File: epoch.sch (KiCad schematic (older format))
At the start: 34 parts, among them J1 USB_OTG, J2 CONN_01X05, J3 CONN_01X02, P3 CONN_01X10, SW1 SW_Reset, U1 MIC5219-3.3BM5, U2 ATSAMD21Ennc-AU, U3 DS3231MZ, U4 MCP7940N-I/SN, U5 74HC1G14GW, U6 MH2mm, U7 MH2mm, U8 MH2mm, U9 MH2mm

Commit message: Remove connector and redo the connections
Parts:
- removed J3: CONN_01X02, Pin_Headers:Pin_Header_Straight_1x02_Pitch1.27mm, symbol CONN_01X02
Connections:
- net labels removed: +3.3V(BATT), +3.3V(REGUL)
- wire segments 110 -> 105
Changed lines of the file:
@@
 Wire Wire Line
 	6650 950  6650 850
-Wire Wire Line
-	4800 2300 4950 2300
-Text GLabel 5050 1250 2    60   Output ~ 0
-+3.3V(REGUL)
 Text GLabel 2550 4400 0    60   Input ~ 0
 SWDIO
@@
 Wire Wire Line
 	8800 5600 9000 5600
-Text GLabel 4950 2300 2    60   Output ~ 0
-+3.3V(BATT)
 Text GLabel 2550 4500 0    60   Input ~ 0
 SWDCLK
-$Comp
-L CONN_01X02 J3
-U 1 1 5A087ADC
-P 10750 5550
-F 0 "J3" H 10750 5700 50  0000 C CNN
-F 1 "CONN_01X02" V 10850 5550 50  0000 C CNN
-F 2 "Pin_Headers:Pin_Header_Straight_1x02_Pitch1.27mm" H 10750 5550 50  0001 C CNN
-F 3 "" H 10750 5550 50  0001 C CNN
-	1    10750 5550
-	1    0    0    -1
-$EndComp
-Text GLabel 10450 5500 0    60   Input ~ 0
-+3.3V(REGUL)
-Text GLabel 10450 5650 0    60   Input ~ 0
-+3.3V(BATT)
-Wire Wire Line
-	10550 5500 10450 5500
-Wire Wire Line
-	10550 5600 10500 5600
-Wire Wire Line
-	10500 5600 10500 5650
-Wire Wire Line
-	10500 5650 10450 5650
 $Comp
 L (GND) #PWR033
@@
 Wire Wire Line
 	5300 7100 5400 7100
+$Comp
+L (+3.3) #PWR034
+U 1 1 5BC006BD
+P 4800 2300
+F 0 "#PWR034" H 4800 2350 30  0001 C CNN
+F 1 "(+3.3)" H 4800 2400 50  0000 C CNN
+F 2 "" H 4800 2300 60  0000 C CNN
+F 3 "" H 4800 2300 60  0000 C CNN
+	1    4800 2300
+	1    0    0    -1
+$EndComp
+$Comp
+L (+3.3) #PWR035
+U 1 1 5BC00ACB
+P 5050 1250
+F 0 "#PWR035" H 5050 1300 30  0001 C CNN
+F 1 "(+3.3)" H 5050 1350 50  0000 C CNN
+F 2 "" H 5050 1250 60  0000 C CNN
+F 3 "" H 5050 1250 60  0000 C CNN
+	1    5050 1250
+	1    0    0    -1
+$EndComp
 $EndSCHEMATC

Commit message: Update for LIPO power_board
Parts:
- removed BT1: Battery_Cell, Connectors:CR2032-001, symbol Battery_Cell
- removed C11, C2: 0.1uF, Capacitors_SMD:C_0805_HandSoldering, symbol C_Small
- removed P3: CONN_01X10, my-fp-library:MOLEX_0.5MM_505278, symbol CONN_01X10
- removed SW1: SW_Reset, Buttons_Switches_SMD:SW_SPST_B3U-3000P, symbol SW_Push
- removed U1: MIC5219-3.3BM5, TO_SOT_Packages_SMD:SOT-23-5, symbol AP131-33
- removed U5: 74HC1G14GW, TO_SOT_Packages_SMD:SOT-353_SC-70-5_Handsoldering, symbol 74HC1G14GW
- added C11, C2: 0.1uF, Capacitors_SMD:C_0805_HandSoldering, symbol Device:C_Small
- added J3: CONN_01X05, my-fp-library:Pin_Header_Straight_1x05_Pitch1.27mm_no_silk, symbol conn:CONN_01X05
- added P3: CONN_01X10, my-fp-library:MOLEX_0.5MM_505278, symbol conn:CONN_01X10
- added SW1: SW_Reset, Buttons_Switches_SMD:SW_SPST_B3U-3000P, symbol switches:SW_Push
- added U1: MIC5219-3.3BM5, TO_SOT_Packages_SMD:SOT-23-5, symbol regul:AP131-33
- added U5: 74HC1G14GW, TO_SOT_Packages_SMD:SOT-353_SC-70-5_Handsoldering, symbol marks:74HC1G14GW
- C1, C14, C3, C4, C5, C6, C9: symbol C_Small -> Device:C_Small
- D1: symbol LED -> Device:LED
- DOWN1, MID1, UP1: symbol Tact_SW_3x6x33.5 -> marks:Tact_SW_3x6x33.5
- J1: symbol USB_OTG -> conn:USB_OTG
- J2: symbol CONN_01X05 -> conn:CONN_01X05
- R1, R2, R3, R4, R5, R6: symbol R -> Device:R
- U2: symbol ATSAMD21Ennc-AU -> Atmel:ATSAMD21Ennc-AU
- U3: symbol DS3231MZ -> maxim:DS3231MZ
- U4: symbol MCP7940N-I/SN -> epoch-rescue:MCP7940N-I_SN
- U6, U7, U8, U9: symbol MH2.1mm -> marks:MH2.1mm
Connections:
- net (+3.3): now also C11.1, C2.1, P3.5 (P5), P3.6 (P6), P3.7 (P7), U1.5 (OUT), U5.5 (VCC)
- net (GND): now also C11.2, C2.2, J3.1 (P1), P3.10 (P10), P3.9 (P9), SW1.2, U1.2 (GND), U5.3 (GND)
- net EXTMODE: now also P3.8 (P8)
- net SPI_CLK: now also P3.1 (P1)
- net SPI_CS: now also P3.3 (P3)
- net SPI_SI: now also P3.2 (P2)
- net VCOM: now also P3.4 (P4), U5.4 (Y)
- net STAT: now reaches U2.11 (PA08)
- net STAT: now also J3.3 (P3)
- net PWR_SENSE: now reaches U2.8 (PA07)
- net PWR_SENSE: now also J3.2 (P2)
- net at C5.2: now also U1.4 (BP)
- net at R1.1: now also SW1.1
- net at R5.2, U4.7 (MFP): now also U5.2 (A)
- net VCC renamed VSS
- net VSS: now also J3.4 (P4)
- new net (+5): J3.5 (P5), U1.1 (IN), U1.3 (EN)
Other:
- moved on the sheet: C1, C14, C3, C4, C5, C6, C9, DOWN1, J1, MID1, R1, R2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

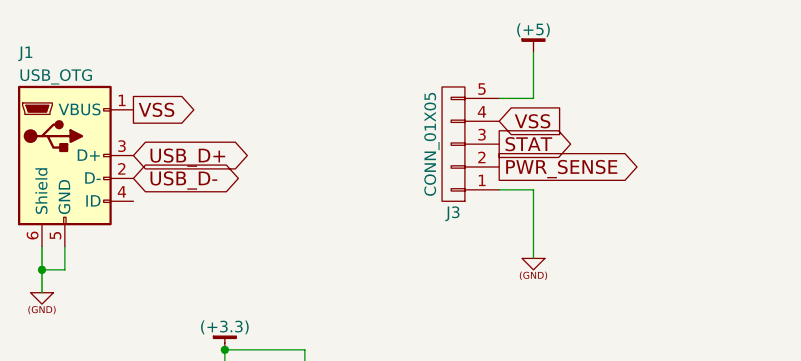
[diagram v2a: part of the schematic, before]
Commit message: New connections to power board
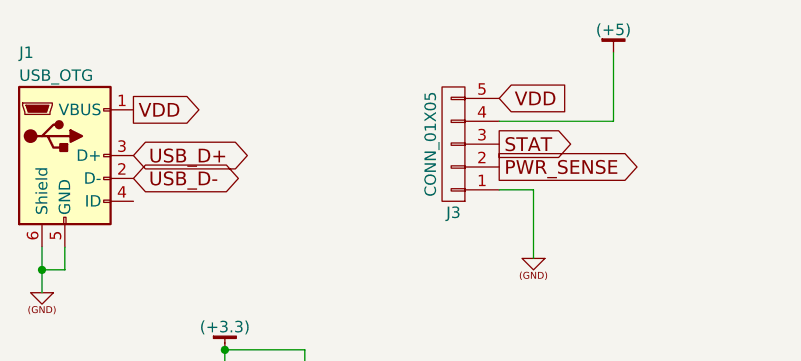
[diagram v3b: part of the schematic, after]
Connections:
- net (+5): now also J3.4 (P4); no longer J3.5 (P5)
- net VSS renamed VDD
- net VDD: now also J3.5 (P5); no longer J3.4 (P4)
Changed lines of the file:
@@
 $EndComp
 Text GLabel 1200 1200 2    60   Output ~ 0
-VSS
+VDD
 $Comp
 L conn:CONN_01X05 J3
@@
 	-1   0    0    -1
 $EndComp
-Text GLabel 2800 1250 2    60   Input ~ 0
-VSS
+Text GLabel 2800 1150 2    60   Input ~ 0
+VDD
 Text GLabel 2800 1350 2    60   Output ~ 0
 STAT
@@
 L power1:(+5) #PWR0102
 U 1 1 5C2AB633
-P 2950 950
-F 0 "#PWR0102" H 2950 1000 30  0001 C CNN
-F 1 "(+5)" H 2950 1050 50  0000 C CNN
-F 2 "" H 2950 950 60  0000 C CNN
-F 3 "" H 2950 950 60  0000 C CNN
-	1    2950 950
+P 3300 950
+F 0 "#PWR0102" H 3300 1000 30  0001 C CNN
+F 1 "(+5)" H 3300 1050 50  0000 C CNN
+F 2 "" H 3300 950 60  0000 C CNN
+F 3 "" H 3300 950 60  0000 C CNN
+	1    3300 950
 	1    0    0    -1
 $EndComp
@@
 Wire Wire Line
 	2950 1550 2950 1850
-Wire Wire Line
-	2800 1150 2950 1150
-Wire Wire Line
-	2950 1150 2950 950
 Text GLabel 3250 3500 2    60   Input ~ 0
 STAT
 Text GLabel 3250 3400 2    60   Input ~ 0
 PWR_SENSE
+Wire Wire Line
+	2800 1250 3300 1250
+Wire Wire Line
+	3300 1250 3300 950
 $EndSCHEMATC

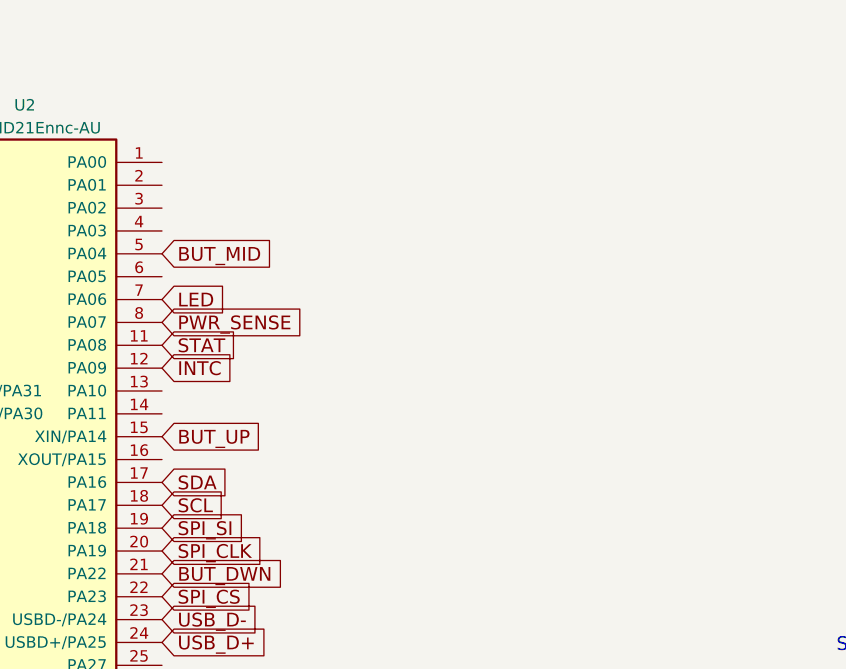
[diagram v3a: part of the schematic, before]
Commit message: Update for voltage divider to get battery level
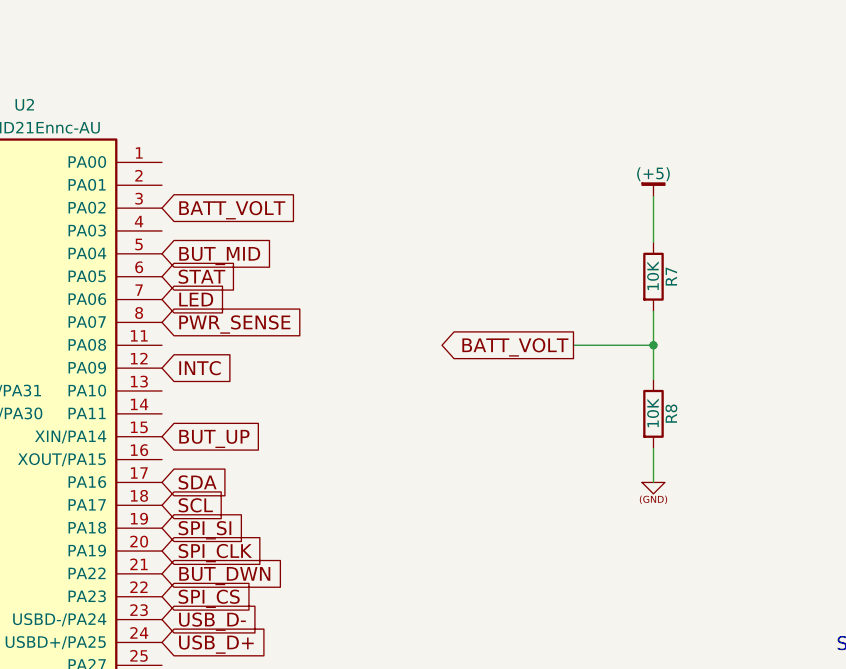
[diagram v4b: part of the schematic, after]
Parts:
- added R7, R8: 10K, Resistors_SMD:R_0805_HandSoldering, symbol Device:R
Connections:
- net (+5): now also R7.1
- net (GND): now also R8.2
- net STAT: now also U2.6 (PA05); no longer U2.11 (PA08)
- net BATT_VOLT: now reaches U2.3 (PA02)
- net BATT_VOLT: now also R7.2, R8.1
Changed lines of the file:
@@
 Wire Wire Line
 	2950 1550 2950 1850
-Text GLabel 3250 3500 2    60   Input ~ 0
+Text GLabel 3250 3200 2    60   Input ~ 0
 STAT
 Text GLabel 3250 3400 2    60   Input ~ 0
@@
 Wire Wire Line
 	3300 1250 3300 950
+$Comp
+L Device:R R8
+U 1 1 5C931DE5
+P 5400 3800
+F 0 "R8" V 5480 3800 50  0000 C CNN
+F 1 "10K" V 5400 3800 50  0000 C CNN
+F 2 "Resistors_SMD:R_0805_HandSoldering" V 5330 3800 50  0001 C CNN
+F 3 "" H 5400 3800 50  0000 C CNN
+	1    5400 3800
+	1    0    0    -1
+$EndComp
+$Comp
+L Device:R R7
+U 1 1 5C936340
+P 5400 3200
+F 0 "R7" V 5480 3200 50  0000 C CNN
+F 1 "10K" V 5400 3200 50  0000 C CNN
+F 2 "Resistors_SMD:R_0805_HandSoldering" V 5330 3200 50  0001 C CNN
+F 3 "" H 5400 3200 50  0000 C CNN
+	1    5400 3200
+	1    0    0    -1
+$EndComp
+$Comp
+L power1:(GND) #PWR0103
+U 1 1 5C93A935
+P 5400 4100
+F 0 "#PWR0103" H 5400 4100 30  0001 C CNN
+F 1 "(GND)" H 5400 4100 30  0001 C CNN
+F 2 "" H 5400 4100 60  0000 C CNN
+F 3 "" H 5400 4100 60  0000 C CNN
+	1    5400 4100
+	1    0    0    -1
+$EndComp
+Wire Wire Line
+	5400 3950 5400 4100
+$Comp
+L power1:(+5) #PWR0104
+U 1 1 5C93F074
+P 5400 2850
+F 0 "#PWR0104" H 5400 2900 30  0001 C CNN
+F 1 "(+5)" H 5400 2950 50  0000 C CNN
+F 2 "" H 5400 2850 60  0000 C CNN
+F 3 "" H 5400 2850 60  0000 C CNN
+	1    5400 2850
+	1    0    0    -1
+$EndComp
+Wire Wire Line
+	5400 2850 5400 3050
+Wire Wire Line
+	5400 3350 5400 3500
+Text GLabel 3250 2900 2    60   Input ~ 0
+BATT_VOLT
+Text GLabel 5050 3500 0    60   Output ~ 0
+BATT_VOLT
+Wire Wire Line
+	5050 3500 5400 3500
+Connection ~ 5400 3500
+Wire Wire Line
+	5400 3500 5400 3650
 $EndSCHEMATC
